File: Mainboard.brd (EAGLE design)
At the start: 90.2 x 95.9 mm, 80 parts, among them J1 POWER_JACKPTH_LOCK, T1 MOSFET_PCHAN_20A, T10 SINGLE_NCHAN_FET, T2 SINGLE_NCHAN_FET, T3 MOSFET_PCHAN_20A, T4 SINGLE_NCHAN_FET, T5 MOSFET_PCHAN_20A, T6 SINGLE_NCHAN_FET, T7 MOSFET_PCHAN_20A, T8 SINGLE_NCHAN_FET, T9 MOSFET_PCHAN_20A, U1 RFM23BP, U2 ARDUINO_PRO_MINI, U3 HMC5883LSMD, U4 TEENSY_3.0+4, U5 ITG-3200, U6 CURRENT_MAX4372, U7 MURATA_REG_OKL-T3-W12, U8 CURRENT_MAX4372

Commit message: Changed R4 value on mainboard
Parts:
- R4: value 120k -> 110k
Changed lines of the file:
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@@
 <element name="R2" library="SparkFun-Resistors" package="0805" value="4.7k" x="57.6" y="76.7" rot="R90"/>
 <element name="R3" library="SparkFun-Resistors" package="0805" value="4.7k" x="57.6" y="72.2" rot="R270"/>
-<element name="R4" library="SparkFun-Resistors" package="0805" value="120k" x="56.5" y="63.2" rot="R90"/>
+<element name="R4" library="SparkFun-Resistors" package="0805" value="110k" x="56.5" y="63.2" rot="R90"/>
 <element name="R5" library="SparkFun-Resistors" package="0805" value="68k" x="56.5" y="59.7" rot="R90"/>
 <element name="C7" library="SparkFun-Capacitors" package="0805" value="2.2nF" x="61.04" y="84.95" smashed="yes" rot="R180">

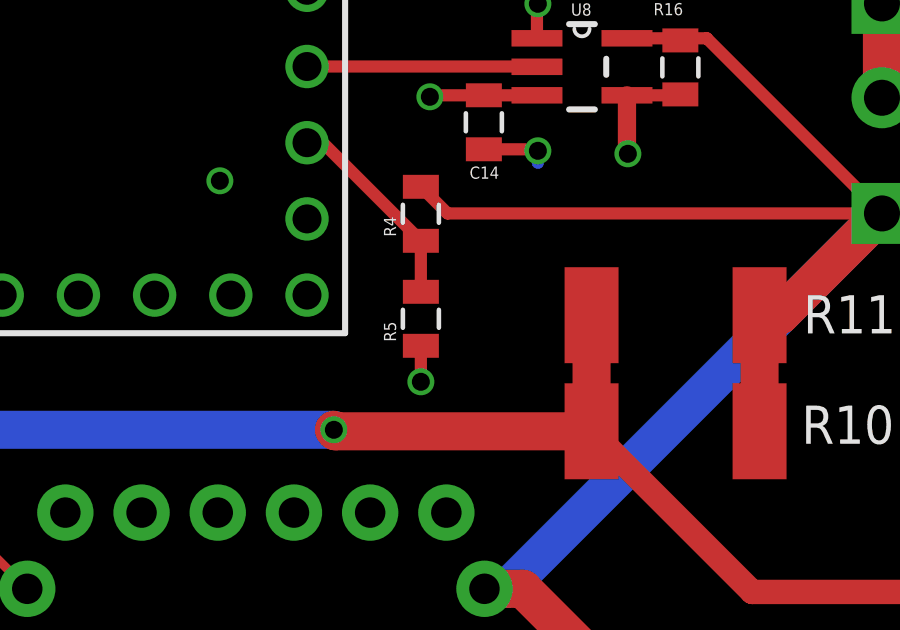
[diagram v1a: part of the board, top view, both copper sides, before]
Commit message: Added cap to battery voltage divider ADC input
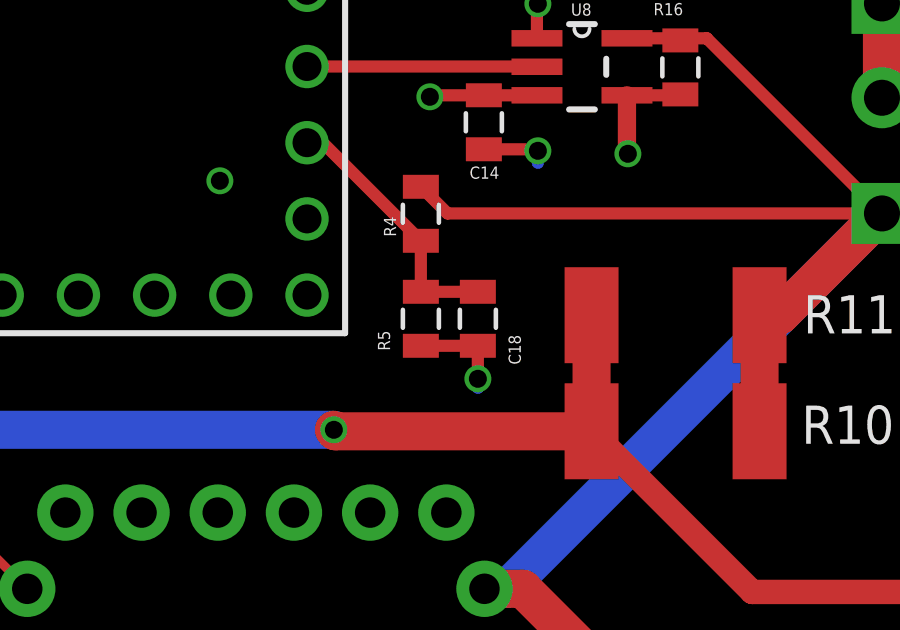
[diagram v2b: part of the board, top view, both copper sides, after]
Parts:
- added C18: 0.1uF, SparkFun-Capacitors:0805
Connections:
- net GND: now also C18.2
- net N$37: now also C18.1
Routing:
- net GND: track 100.0 -> 101.9 mm
- net N$37: track 6.85 -> 8.75 mm
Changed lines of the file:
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@@
 <element name="R3" library="SparkFun-Resistors" package="0805" value="4.7k" x="57.6" y="72.2" rot="R270"/>
 <element name="R4" library="SparkFun-Resistors" package="0805" value="110k" x="56.5" y="63.2" rot="R90"/>
-<element name="R5" library="SparkFun-Resistors" package="0805" value="68k" x="56.5" y="59.7" rot="R90"/>
+<element name="R5" library="SparkFun-Resistors" package="0805" value="68k" x="56.5" y="59.7" smashed="yes" rot="R90">
+<attribute name="NAME" x="55.4745" y="58.638" size="0.4064" layer="25" rot="R90"/>
+<attribute name="VALUE" x="55.497" y="60.084" size="0.4064" layer="27" rot="R90"/>
+</element>
 <element name="C7" library="SparkFun-Capacitors" package="0805" value="2.2nF" x="61.04" y="84.95" smashed="yes" rot="R180">
 <attribute name="NAME" x="61.802" y="84.1245" size="0.4064" layer="25" rot="R180"/>
@@
 <element name="JP7" library="SparkFun-Connectors" package="MOLEX-1X3_LOCK" value="" x="73.3" y="4.5" smashed="yes"/>
 <element name="U$3" library="KickSat-Logo" package="KICKSAT_LOGO" value="KICKSAT_LOGO" x="22.3" y="21.4" rot="MR90"/>
+<element name="C18" library="SparkFun-Capacitors" package="0805" value="0.1uF" x="58.4" y="59.7" smashed="yes" rot="R270">
+<attribute name="NAME" x="59.4255" y="59.162" size="0.4064" layer="25" rot="R270"/>
+<attribute name="VALUE" x="59.403" y="61.216" size="0.4064" layer="27" rot="R270"/>
+</element>
 </elements>
 <signals>
@@
 <contactref element="U1" pad="GND1"/>
 <contactref element="U4" pad="AGND"/>
-<contactref element="R5" pad="1"/>
 <contactref element="U5" pad="18"/>
 <contactref element="U5" pad="1"/>
@@
 <wire x1="58.6" y1="65.35" x2="60.35" y2="65.35" width="0.4064" layer="1"/>
 <wire x1="60.35" y1="65.35" x2="60.4" y2="65.3" width="0.4064" layer="1"/>
-<wire x1="56.5" y1="58.8" x2="56.5" y2="57.6" width="0.4064" layer="1"/>
-<via x="56.5" y="57.6" extent="1-16" drill="0.6"/>
-<wire x1="56.5" y1="57.6" x2="56.5" y2="57.4" width="0.4064" layer="16"/>
 <wire x1="24.8" y1="8.7" x2="24.8" y2="6.2" width="0.4064" layer="1"/>
 <wire x1="24.8" y1="6.2" x2="25.2" y2="5.8" width="0.4064" layer="1"/>
 <via x="25.2" y="5.8" extent="1-16" drill="0.6"/>
 <wire x1="25.2" y1="5.8" x2="25.5" y2="5.8" width="0.4064" layer="16"/>
+<contactref element="R5" pad="1"/>
+<contactref element="C18" pad="2"/>
+<wire x1="56.5" y1="58.8" x2="58.4" y2="58.8" width="0.4064" layer="1"/>
+<wire x1="58.4" y1="58.8" x2="58.4" y2="57.7" width="0.4064" layer="1"/>
+<via x="58.4" y="57.7" extent="1-16" drill="0.6"/>
+<wire x1="58.4" y1="57.7" x2="58.4" y2="57.4" width="0.4064" layer="16"/>
 </signal>
 <signal name="VREG_IN">
@@
 <signal name="N$37">
 <contactref element="R4" pad="1"/>
-<contactref element="R5" pad="2"/>
 <contactref element="U4" pad="15/A1"/>
 <wire x1="52.705" y1="65.57" x2="53.23" y2="65.57" width="0.4064" layer="1"/>
 <wire x1="53.23" y1="65.57" x2="56.5" y2="62.3" width="0.4064" layer="1"/>
-<wire x1="56.5" y1="60.6" x2="56.5" y2="62.3" width="0.4064" layer="1"/>
+<contactref element="R5" pad="2"/>
+<contactref element="C18" pad="1"/>
+<wire x1="56.5" y1="62.3" x2="56.5" y2="60.6" width="0.4064" layer="1"/>
+<wire x1="56.5" y1="60.6" x2="58.4" y2="60.6" width="0.4064" layer="1"/>
 </signal>
 <signal name="N$39">

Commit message: Changed voltage divider resistor values
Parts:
- R4: value 110k -> 316k
- R5: value 68k -> 110k
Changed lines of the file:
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@@
 <element name="R2" library="SparkFun-Resistors" package="0805" value="4.7k" x="57.6" y="76.7" rot="R90"/>
 <element name="R3" library="SparkFun-Resistors" package="0805" value="4.7k" x="57.6" y="72.2" rot="R270"/>
-<element name="R4" library="SparkFun-Resistors" package="0805" value="110k" x="56.5" y="63.2" rot="R90"/>
-<element name="R5" library="SparkFun-Resistors" package="0805" value="68k" x="56.5" y="59.7" smashed="yes" rot="R90">
+<element name="R4" library="SparkFun-Resistors" package="0805" value="316k" x="56.5" y="63.2" rot="R90"/>
+<element name="R5" library="SparkFun-Resistors" package="0805" value="110k" x="56.5" y="59.7" smashed="yes" rot="R90">
 <attribute name="NAME" x="55.4745" y="58.638" size="0.4064" layer="25" rot="R90"/>
 <attribute name="VALUE" x="55.497" y="60.084" size="0.4064" layer="27" rot="R90"/>

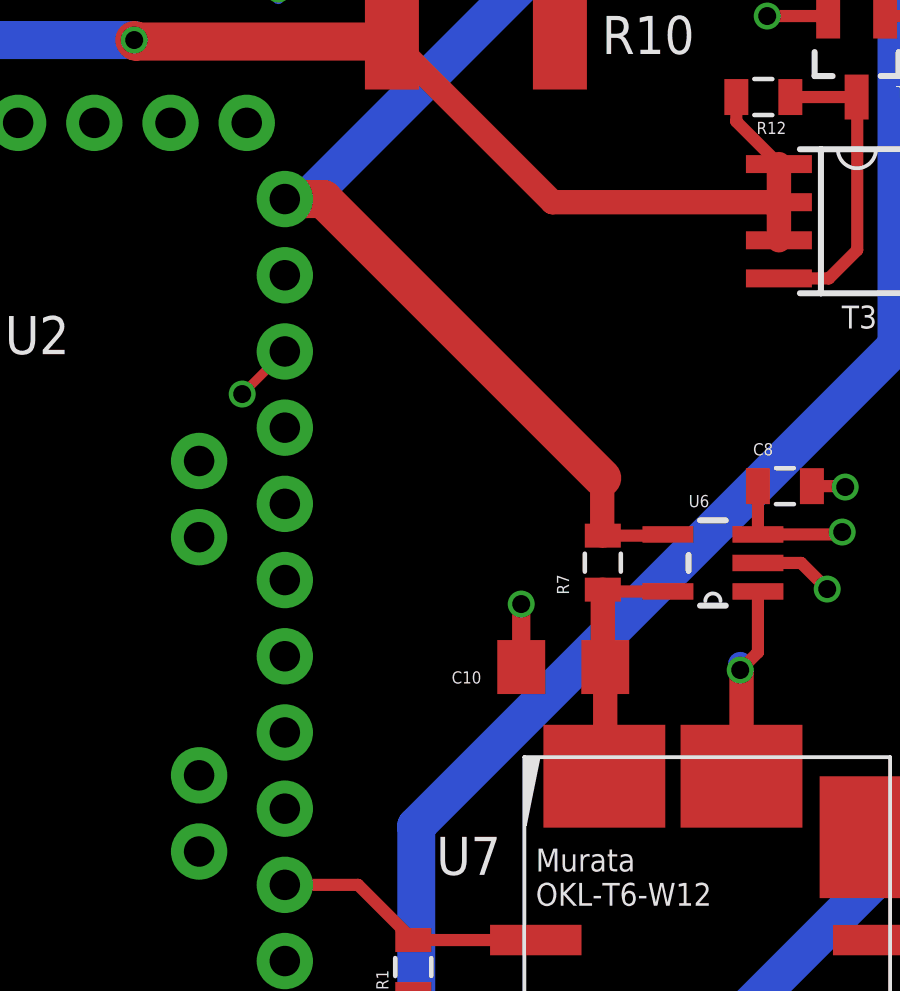
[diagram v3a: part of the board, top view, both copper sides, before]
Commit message: Added battery voltage monitoring to arduino
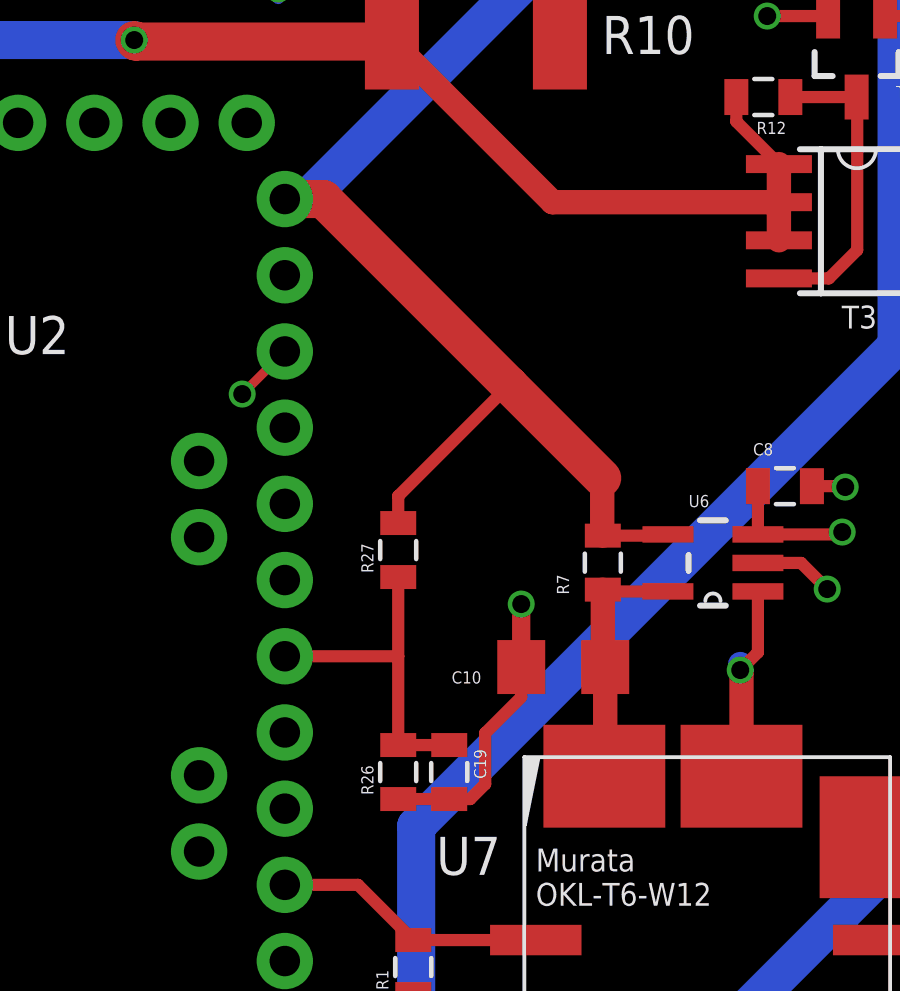
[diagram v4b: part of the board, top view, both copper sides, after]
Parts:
- added C19: 0.1uF, SparkFun-Capacitors:0805
- added R26, R27: 100k, SparkFun-Resistors:0805
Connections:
- new net N$17: C19.1, R26.2, R27.1, U2.18
- net GND: now also C19.2, R26.1
- net VBATT: now also R27.2
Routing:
- net N$17: track 0.00 -> 11.1 mm
- net GND: track 101.9 -> 109.5 mm
- net VBATT: track 73.1 -> 79.2 mm
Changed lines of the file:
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@@
 <attribute name="VALUE" x="59.403" y="61.216" size="0.4064" layer="27" rot="R270"/>
 </element>
+<element name="R26" library="SparkFun-Resistors" package="0805" value="100k" x="62.4" y="31.6" rot="R90"/>
+<element name="R27" library="SparkFun-Resistors" package="0805" value="100k" x="62.4" y="39" rot="R90"/>
+<element name="C19" library="SparkFun-Capacitors" package="0805" value="0.1uF" x="64.1" y="31.6" rot="R270"/>
 </elements>
 <signals>
@@
 <via x="58.4" y="57.7" extent="1-16" drill="0.6"/>
 <wire x1="58.4" y1="57.7" x2="58.4" y2="57.4" width="0.4064" layer="16"/>
+<contactref element="R26" pad="1"/>
+<contactref element="C19" pad="2"/>
+<wire x1="62.4" y1="30.7" x2="64.1" y2="30.7" width="0.4064" layer="1"/>
+<wire x1="66.5" y1="35.1" x2="66.5" y2="34.1" width="0.4064" layer="1"/>
+<wire x1="66.5" y1="34.1" x2="65.3" y2="32.9" width="0.4064" layer="1"/>
+<wire x1="65.3" y1="32.9" x2="65.3" y2="31.2" width="0.4064" layer="1"/>
+<wire x1="65.3" y1="31.2" x2="64.8" y2="30.7" width="0.4064" layer="1"/>
+<wire x1="64.8" y1="30.7" x2="64.1" y2="30.7" width="0.4064" layer="1"/>
 </signal>
 <signal name="VREG_IN">
@@
 <wire x1="59.3578" y1="50.7" x2="58.62" y2="50.7" width="1.27" layer="16"/>
 <wire x1="58.62" y1="50.7" x2="59.9" y2="50.7" width="1.27" layer="1"/>
-<wire x1="59.9" y1="50.7" x2="69.2" y2="41.4" width="1.27" layer="1"/>
+<wire x1="59.9" y1="50.7" x2="66.1" y2="44.5" width="1.27" layer="1"/>
+<wire x1="66.1" y1="44.5" x2="69.2" y2="41.4" width="1.27" layer="1"/>
 <wire x1="69.2" y1="41.4" x2="69.2" y2="39.5" width="0.8128" layer="1"/>
 <wire x1="69.2" y1="39.5" x2="69.22" y2="39.48" width="0.8128" layer="1"/>
@@
 <wire x1="71.87" y1="63.2122" x2="68.4778" y2="59.82" width="1.27" layer="1"/>
 <wire x1="68.4778" y1="59.82" x2="67.79" y2="59.82" width="1.27" layer="1"/>
+<contactref element="R27" pad="2"/>
+<wire x1="62.4" y1="39.9" x2="62.4" y2="40.8" width="0.4064" layer="1"/>
+<wire x1="62.4" y1="40.8" x2="66.1" y2="44.5" width="0.4064" layer="1"/>
 </signal>
 <signal name="VBAT">
@@
 </polygon>
 </signal>
+<signal name="N$17">
+<contactref element="U2" pad="18"/>
+<contactref element="C19" pad="1"/>
+<contactref element="R26" pad="2"/>
+<contactref element="R27" pad="1"/>
+<wire x1="58.62" y1="35.46" x2="62.4" y2="35.46" width="0.4064" layer="1"/>
+<wire x1="62.4" y1="35.46" x2="62.4" y2="32.5" width="0.4064" layer="1"/>
+<wire x1="62.4" y1="32.5" x2="64.1" y2="32.5" width="0.4064" layer="1"/>
+<wire x1="62.4" y1="35.46" x2="62.4" y2="38.1" width="0.4064" layer="1"/>
+</signal>
 </signals>
